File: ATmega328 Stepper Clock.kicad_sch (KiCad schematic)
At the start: 18 parts, among them J1 5750071-1, J2 SBH11-PBPC-D05-ST-BK, J4 MMS-103-01-L-DV, M1 Stepper_Motor_bipolar, M2 Stepper_Motor_bipolar, Q1 TCRT5000, Q2 TCRT5000, U1 ATMEGA328P-AU, Y1 Crystal

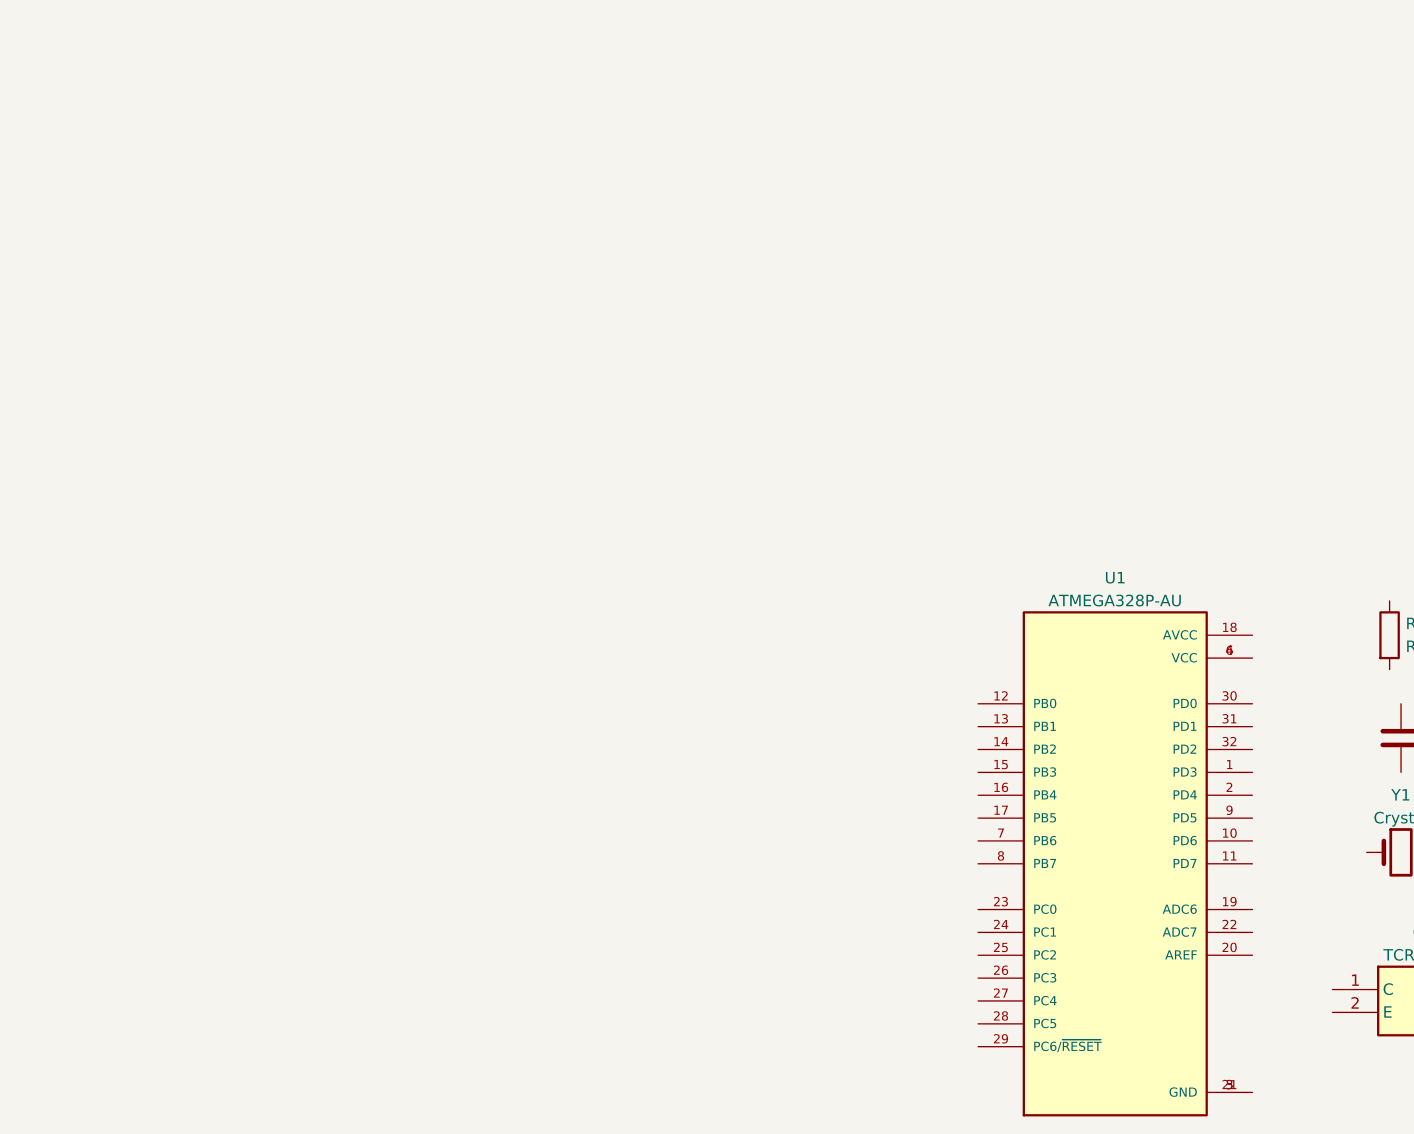
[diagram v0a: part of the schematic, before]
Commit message: changed ATmega328P-AU to ATmega328-au
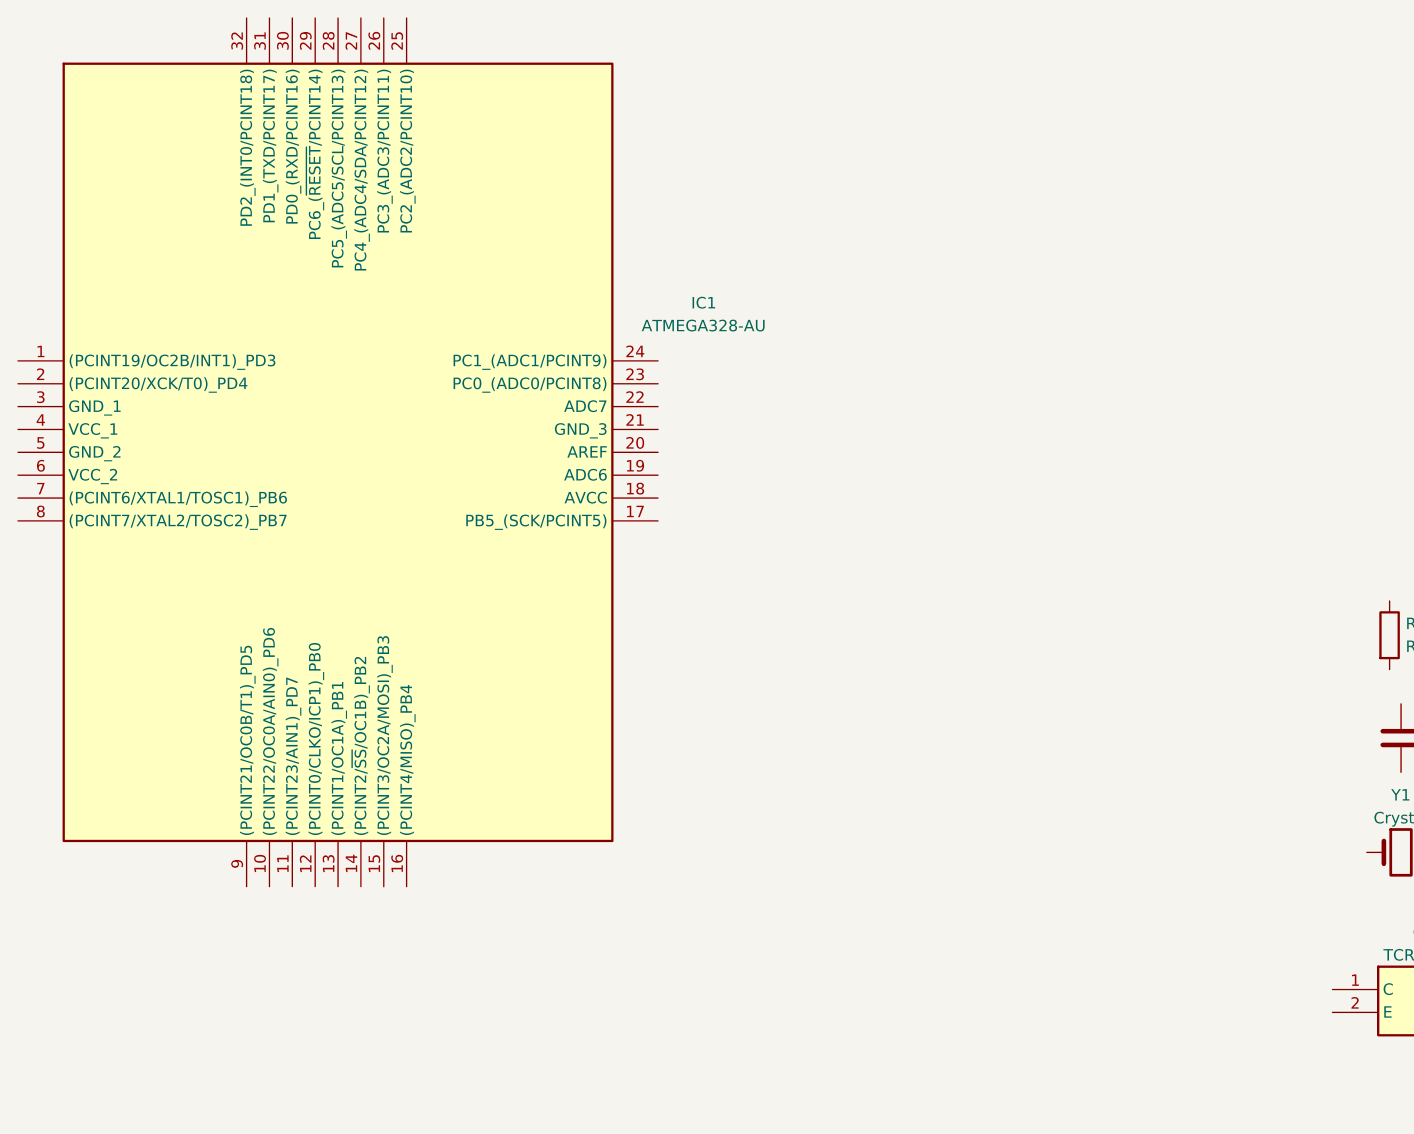
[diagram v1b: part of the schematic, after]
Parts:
- removed U1: ATMEGA328P-AU, ATMEGA328P-AU:QFP80P900X900X120-32N, symbol ATMEGA328P-AU:ATMEGA328P-AU
- added IC1: ATMEGA328-AU, QFP80P900X900X120-32N, symbol SamacSys_Parts:ATMEGA328-AU
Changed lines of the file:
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@@
+	)
+	(symbol
+		(lib_id "SamacSys_Parts:ATMEGA328-AU")
+		(at -190.5 -167.64 0)
+		(unit 1)
+		(exclude_from_sim no)
+		(in_bom yes)
+		(on_board yes)
+		(dnp no)
+		(fields_autoplaced yes)
+		(property "Reference" "IC1"
+			(at -114.3 -174.0602 0)
+			(effects
+				(font
+					(size 1.27 1.27)
+				)
+			)
+		)
+		(property "Value" "ATMEGA328-AU"
+			(at -114.3 -171.5202 0)
+			(effects
+				(font
+					(size 1.27 1.27)
+				)
+			)
+		)
+		(property "Footprint" "QFP80P900X900X120-32N"
+			(at -123.19 -103.2 0)
+			(effects
+				(font
+					(size 1.27 1.27)
+				)
+				(justify left top)
+				(hide yes)
+			)
+		)
+		(property "Datasheet" "https://ww1.microchip.com/downloads/en/DeviceDoc/ATmega48A-PA-88A-PA-168A-PA-328-P-DS-DS40002061B.pdf"
+			(at -123.19 -3.2 0)
+			(effects
+				(font
+					(size 1.27 1.27)
+				)
+				(justify left top)
+				(hide yes)
+			)
+		)
+		(property "Description" "MCU 8-Bit AVR 32KB Flash 2.5/3.3/5V ATMEGA328-AU, 8 bit AVR Microcontroller 20MHz 32 kB Flash, 1 kB, 2 kB RAM, I2C 32-Pin TQFP"
+			(at -190.5 -167.64 0)
+			(effects
+				(font
+					(size 1.27 1.27)
+				)
+				(hide yes)
+			)
+		)
+		(property "Height" "1.2"
+			(at -123.19 196.8 0)
+			(effects
+				(font
+					(size 1.27 1.27)
+				)
+				(justify left top)
+				(hide yes)
+			)
+		)
+		(property "Manufacturer_Name" "Microchip"
+			(at -123.19 296.8 0)
+			(effects
+				(font
+					(size 1.27 1.27)
+				)
+				(justify left top)
+				(hide yes)
+			)
+		)
+		(property "Manufacturer_Part_Number" "ATMEGA328-AU"
+			(at -123.19 396.8 0)
+			(effects
+				(font
+					(size 1.27 1.27)
+				)
+				(justify left top)
+				(hide yes)
+			)
+		)
+		(property "Mouser Part Number" "556-ATMEGA328-AU"
+			(at -123.19 496.8 0)
+			(effects
+				(font
+					(size 1.27 1.27)
+				)
+				(justify left top)
+				(hide yes)
+			)
+		)
+		(property "Mouser Price/Stock" "https://www.mouser.co.uk/ProductDetail/Microchip-Technology/ATMEGA328-AU?qs=lwdSMh1%2FoYJRHuGBjWz9Pg%3D%3D"
+			(at -123.19 596.8 0)
+			(effects
+				(font
+					(size 1.27 1.27)
+				)
+				(justify left top)
+				(hide yes)
+			)
+		)
+		(property "Arrow Part Number" "ATMEGA328-AU"
+			(at -123.19 696.8 0)
+			(effects
+				(font
+					(size 1.27 1.27)
+				)
+				(justify left top)
+				(hide yes)
+			)
+		)
+		(property "Arrow Price/Stock" "https://www.arrow.com/en/products/atmega328-au/microchip-technology?utm_currency=USD&region=nac"
+			(at -123.19 796.8 0)
+			(effects
+				(font
+					(size 1.27 1.27)
+				)
+				(justify left top)
+				(hide yes)
+			)
+		)
+		(pin "1"
+		)
+		(pin "3"
+		)
+		(pin "5"
+		)
+		(pin "2"
+		)
+		(pin "4"
+		)
+		(pin "6"
+		)
+		(pin "8"
+		)
+		(pin "20"
+		)
+		(pin "12"
+		)
+		(pin "25"
+		)
+		(pin "21"
+		)
+		(pin "29"
+		)
+		(pin "30"
+		)
+		(pin "13"
+		)
+		(pin "7"
+		)
+		(pin "14"
+		)
+		(pin "11"
+		)
+		(pin "31"
+		)
+		(pin "32"
+		)
+		(pin "23"
+		)
+		(pin "10"
+		)
+		(pin "28"
+		)
+		(pin "15"
+		)
+		(pin "27"
+		)
+		(pin "26"
+		)
+		(pin "9"
+		)
+		(pin "16"
+		)
+		(pin "24"
+		)
+		(pin "22"
+		)
+		(pin "19"
+		)
+		(pin "18"
+		)
+		(pin "17"
+		)
+		(instances
+			(project ""
+				(path "/58947f94-6b9d-44b0-813c-e16abdea2252"
+					(reference "IC1")
+					(unit 1)
+				)
+			)
+		)
 	)
 	(symbol
@@
 					(unit 1)
 				)
-			)
-		)
-	)
-	(symbol
-		(lib_id "ATMEGA328P-AU:ATMEGA328P-AU")
-		(at -68.58 -111.76 0)
-		(unit 1)
-		(exclude_from_sim no)
-		(in_bom yes)
-		(on_board yes)
-		(dnp no)
-		(fields_autoplaced yes)
-		(property "Reference" "U1"
-			(at -68.58 -143.51 0)
-			(effects
-				(font
-					(size 1.27 1.27)
-				)
-			)
-		)
-		(property "Value" "ATMEGA328P-AU"
-			(at -68.58 -140.97 0)
-			(effects
-				(font
-					(size 1.27 1.27)
-				)
-			)
-		)
-		(property "Footprint" "ATMEGA328P-AU:QFP80P900X900X120-32N"
-			(at -68.58 -111.76 0)
-			(effects
-				(font
-					(size 1.27 1.27)
-				)
-				(justify bottom)
-				(hide yes)
-			)
-		)
-		(property "Datasheet" ""
-			(at -68.58 -111.76 0)
-			(effects
-				(font
-					(size 1.27 1.27)
-				)
-				(hide yes)
-			)
-		)
-		(property "Description" ""
-			(at -68.58 -111.76 0)
-			(effects
-				(font
-					(size 1.27 1.27)
-				)
-				(hide yes)
-			)
-		)
-		(property "MF" "MICROCHIP TECH."
-			(at -68.58 -111.76 0)
-			(effects
-				(font
-					(size 1.27 1.27)
-				)
-				(justify bottom)
-				(hide yes)
-			)
-		)
-		(property "MAXIMUM_PACKAGE_HEIGHT" "1.20mm"
-			(at -68.58 -111.76 0)
-			(effects
-				(font
-					(size 1.27 1.27)
-				)
-				(justify bottom)
-				(hide yes)
-			)
-		)
-		(property "Package" "TQFP-32 Microchip"
-			(at -68.58 -111.76 0)
-			(effects
-				(font
-					(size 1.27 1.27)
-				)
-				(justify bottom)
-				(hide yes)
-			)
-		)
-		(property "Price" "None"
-			(at -68.58 -111.76 0)
-			(effects
-				(font
-					(size 1.27 1.27)
-				)
-				(justify bottom)
-				(hide yes)
-			)
-		)
-		(property "Check_prices" "https://www.snapeda.com/parts/ATMEGA328P-AU/Microchip+Technology/view-part/?ref=eda"
-			(at -68.58 -111.76 0)
-			(effects
-				(font
-					(size 1.27 1.27)
-				)
-				(justify bottom)
-				(hide yes)
-			)
-		)
-		(property "STANDARD" "IPC-7351B"
-			(at -68.58 -111.76 0)
-			(effects
-				(font
-					(size 1.27 1.27)
-				)
-				(justify bottom)
-				(hide yes)
-			)
-		)
-		(property "PARTREV" "8271A"
-			(at -68.58 -111.76 0)
-			(effects
-				(font
-					(size 1.27 1.27)
-				)
-				(justify bottom)
-				(hide yes)
-			)
-		)
-		(property "SnapEDA_Link" "https://www.snapeda.com/parts/ATMEGA328P-AU/Microchip+Technology/view-part/?ref=snap"
-			(at -68.58 -111.76 0)
-			(effects
-				(font
-					(size 1.27 1.27)
-				)
-				(justify bottom)
-				(hide yes)
-			)
-		)
-		(property "MP" "ATMEGA328P-AU"
-			(at -68.58 -111.76 0)
-			(effects
-				(font
-					(size 1.27 1.27)
-				)
-				(justify bottom)
-				(hide yes)
-			)
-		)
-		(property "Description_1" "MCU 8-bit - AVR ATmega Family ATmega328 Series Microcontrollers - 20 MHz - 32 KB - 2 KB - 32 Pins."
-			(at -68.58 -111.76 0)
-			(effects
-				(font
-					(size 1.27 1.27)
-				)
-				(justify bottom)
-				(hide yes)
-			)
-		)
-		(property "Availability" "In Stock"
-			(at -68.58 -111.76 0)
-			(effects
-				(font
-					(size 1.27 1.27)
-				)
-				(justify bottom)
-				(hide yes)
-			)
-		)
-		(property "MANUFACTURER" "Microchip"
-			(at -68.58 -111.76 0)
-			(effects
-				(font
-					(size 1.27 1.27)
-				)
-				(justify bottom)
-				(hide yes)
-			)
-		)
-		(pin "27"
-		)
-		(pin "14"
-		)
-		(pin "7"
-		)
-		(pin "16"
-		)
-		(pin "8"
-		)
-		(pin "23"
-		)
-		(pin "13"
-		)
-		(pin "24"
-		)
-		(pin "15"
-		)
-		(pin "25"
-		)
-		(pin "17"
-		)
-		(pin "26"
-		)
-		(pin "28"
-		)
-		(pin "4"
-		)
-		(pin "6"
-		)
-		(pin "30"
-		)
-		(pin "31"
-		)
-		(pin "18"
-		)
-		(pin "1"
-		)
-		(pin "9"
-		)
-		(pin "10"
-		)
-		(pin "2"
-		)
-		(pin "11"
-		)
-		(pin "19"
-		)
-		(pin "20"
-		)
-		(pin "22"
-		)
-		(pin "21"
-		)
-		(pin "32"
-		)
-		(pin "3"
-		)
-		(pin "29"
-		)
-		(pin "12"
-		)
-		(pin "5"
-		)
-		(instances
-			(project ""
-				(path "/58947f94-6b9d-44b0-813c-e16abdea2252"
-					(reference "U1")
-					(unit 1)
-				)

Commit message: Rogh schematic connections done
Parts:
- renumbered J1 to DIN, J4 to ISP
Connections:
- net at Y1.1: now also C2.2, IC1.8 ((PCINT7/XTAL2/TOSC2)_PB7)
- net at Y1.2: now also C1.2, IC1.7 ((PCINT6/XTAL1/TOSC1)_PB6)
- net VCC: now reaches R2.1
- net VCC: now also DIN.4, IC1.18 (AVCC), IC1.20 (AREF), IC1.4 (VCC_1), IC1.6 (VCC_2), ISP.3, J2.7, R1.1, R3.1
- net at R2.2: now also Q1.4 (A)
- net SCL: now reaches J2.1
- net SCL: now also DIN.5, IC1.28 (PC5_(ADC5/SCL/PCINT13))
- net GND: now reaches J2.10
- net GND: now also C1.1, C2.1, DIN.3, IC1.21 (GND_3), IC1.3 (GND_1), IC1.5 (GND_2), ISP.6, Q1.2 (E), Q1.3 (K), Q2.2 (E), Q2.3 (K)
- net SDA: now reaches J2.3
- net SDA: now also DIN.1, IC1.27 (PC4_(ADC4/SDA/PCINT12))
- net at R3.2: now also Q2.4 (A)
- net PD3: now reaches IC1.1 ((PCINT19/OC2B/INT1)_PD3)
- net PD3: now also Q2.1 (C)
- net MOT_MINUTE_D: now reaches IC1.12 ((PCINT0/CLKO/ICP1)_PB0)
- net MOT_MINUTE_D: now also M2.D
- net MOT_MINUTE_C: now reaches IC1.13 ((PCINT1/OC1A)_PB1)
- net MOT_MINUTE_C: now also M2.C
- net MOT_MINUTE_A: now reaches IC1.14 ((PCINT2/~{SS}/OC1B)_PB2)
- net MOT_MINUTE_A: now also M2.A
- net MOSI: now reaches IC1.15 ((PCINT3/OC2A/MOSI)_PB3)
- net MOSI: now also ISP.4
- net MISO&MOT_MINUTE_B: now reaches IC1.16 ((PCINT4/MISO)_PB4)
- net MISO&MOT_MINUTE_B: now also ISP.1, M2.B (-)
- net SCK: now reaches IC1.17 (PB5_(SCK/PCINT5))
- net SCK: now also ISP.2
- net MOT_HOUR_B: now reaches IC1.23 (PC0_(ADC0/PCINT8))
- net MOT_HOUR_B: now also M1.B (-)
- net MOT_HOUR_D: now reaches IC1.24 (PC1_(ADC1/PCINT9))
- net MOT_HOUR_D: now also M1.D
- net MOT_HOUR_A: now reaches IC1.25 (PC2_(ADC2/PCINT10))
- net MOT_HOUR_A: now also M1.A
- net MOT_HOUR_C: now reaches IC1.26 (PC3_(ADC3/PCINT11))
- net MOT_HOUR_C: now also M1.C
- net RESET: now reaches IC1.29 (PC6_(~{RESET}/PCINT14))
- net RESET: now also ISP.5, R1.2
- net PD2: now reaches IC1.32 (PD2_(INT0/PCINT18))
- net PD2: now also Q1.1 (C)
- no-connect marks 0 -> 19
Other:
- title: (none) -> ATmega328 Stepper Clock
- moved on the sheet: C1, C2, DIN, IC1, ISP, J2, M1, M2, Q1, Q2, R1, R2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

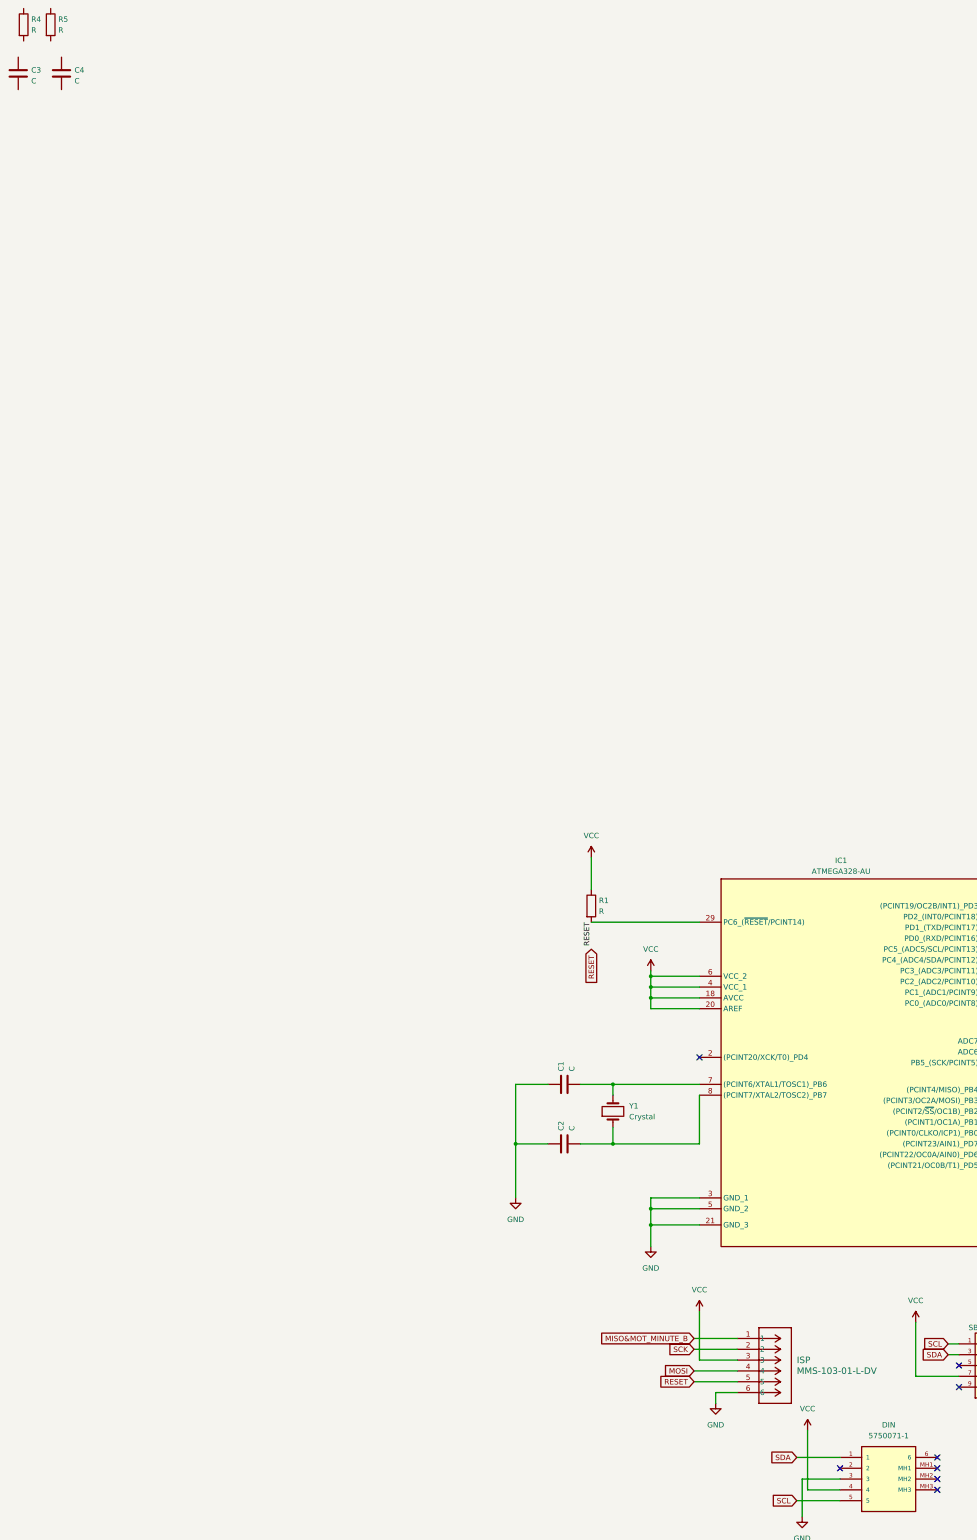
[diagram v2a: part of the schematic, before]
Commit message: Made some changes and assigned footprint for all except stepper motors
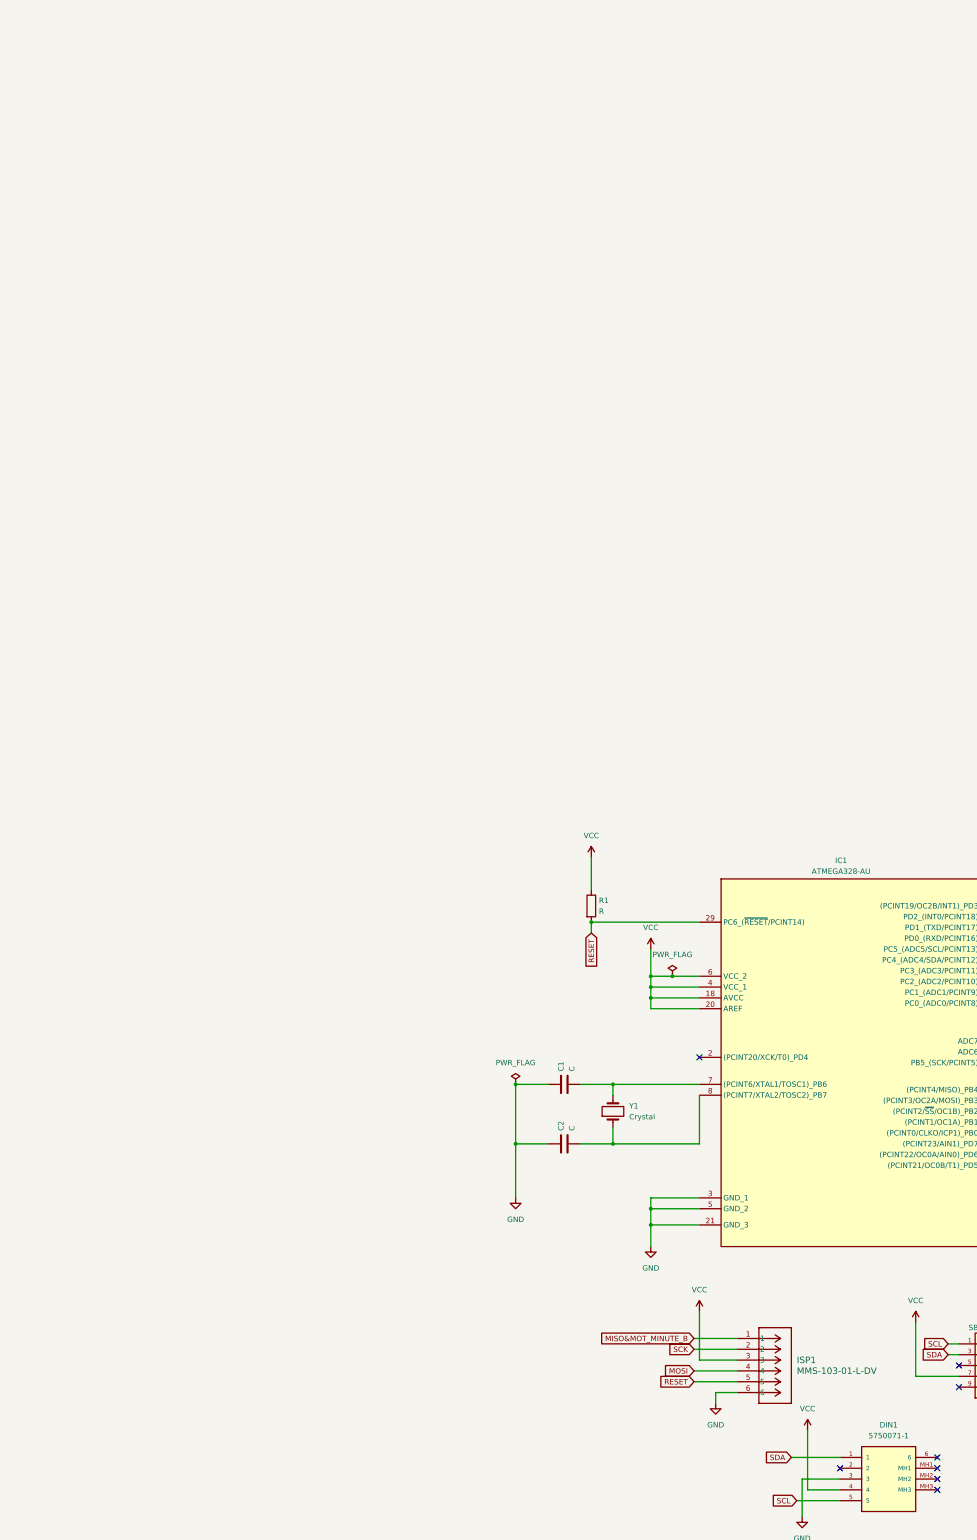
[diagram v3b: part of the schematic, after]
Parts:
- removed C3, C4: C, symbol Device:C
- removed R4, R5: R, symbol Device:R
- C1, C2: footprint (none) -> Capacitor_THT:C_Axial_L5.1mm_D3.1mm_P15.00mm_Horizontal
- IC1: footprint QFP80P900X900X120-32N -> SamacSys_Parts:QFP80P900X900X120-32N
- Q1, Q2: footprint TCRT5000 -> SamacSys_Parts:TCRT5000
- R1, R2, R3: footprint (none) -> Resistor_THT:R_Axial_DIN0414_L11.9mm_D4.5mm_P15.24mm_Horizontal
- Y1: footprint (none) -> Crystal:Crystal_AT310_D3.0mm_L10.0mm_Horizontal
- renumbered DIN to DIN1, ISP to ISP1
